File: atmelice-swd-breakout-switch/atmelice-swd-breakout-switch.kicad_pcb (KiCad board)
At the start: 2 copper layers, 32.8 x 8.4 mm, 3 parts, among them J1 Conn_02x05_Odd_Even, J2 Conn_01x06, SW1 SW_DPDT_x2

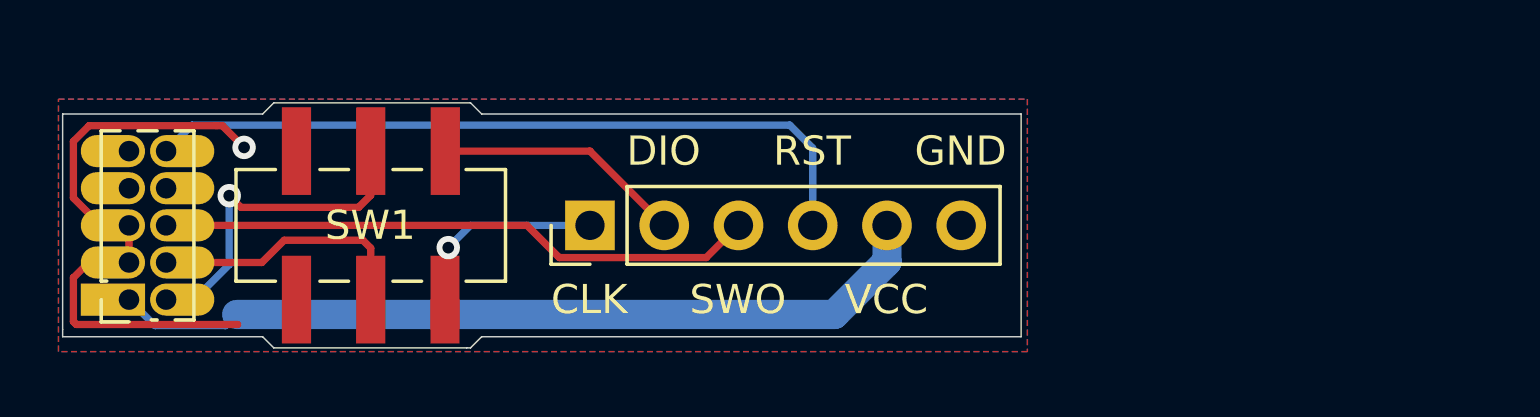
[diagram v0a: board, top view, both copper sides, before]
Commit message: atmelice-swd-breakout-switch: add AVR connector (2021Jan rev)
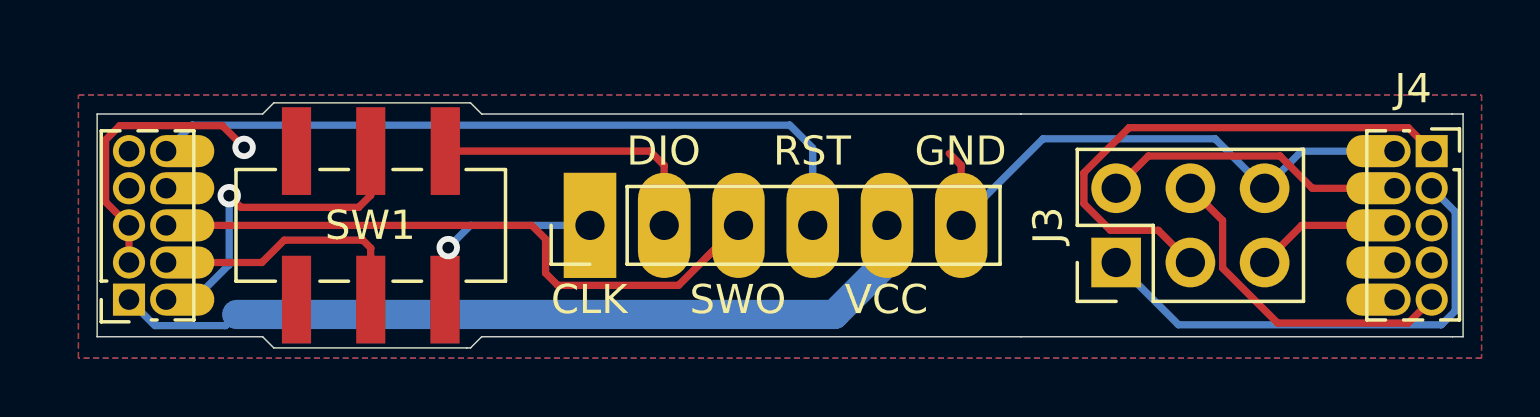
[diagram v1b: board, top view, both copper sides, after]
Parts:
- added J3: Conn_02x03_Odd_Even, tom-connectors:PinHeader_2x03_P2.54mm_Vertical, F.Cu at (159.5, 125.7)
- added J4: AVR, tom-connectors:PinSocket_2x05_P1.27mm_Vertical, F.Cu at (170.3, 121.9)
- J1: value Conn_02x05_Odd_Even -> SAM
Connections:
- net /GND renamed GND
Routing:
- net /AVR_SCK: track 0.00 -> 18.4 mm
- net /AVR_MISO: track 0.00 -> 17.2 mm
- net /AVR_MOSI: track 0.00 -> 11.5 mm
- net /AVR_VTG: track 0.00 -> 10.4 mm
- net GND: track 21.1 -> 31.4 mm
- net /AVR_RESET: track 0.00 -> 4.97 mm
- net /SWO: track 20.5 -> 23.5 mm
- net /SWDIO_2: track 8.54 -> 9.74 mm
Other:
- board size 32.8 x 8.4 mm -> 46.7 x 8.4 mm
- board text added: "Jan2021 @TomKeddie"
- board text removed: "Dec2020 @TomKeddie"

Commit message: atmelice-swd-breakout-switch: fix ground issue, May2023 release
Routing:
- net /SWO: track 23.5 -> 22.0 mm
- net GND: vias 1 -> 2
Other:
- net class Default removed
- board text added: "May2023 @TomKeddie"
- board text added: "ON"
- board text removed: "Jan2021 @TomKeddie"
